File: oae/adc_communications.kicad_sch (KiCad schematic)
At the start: 2 parts

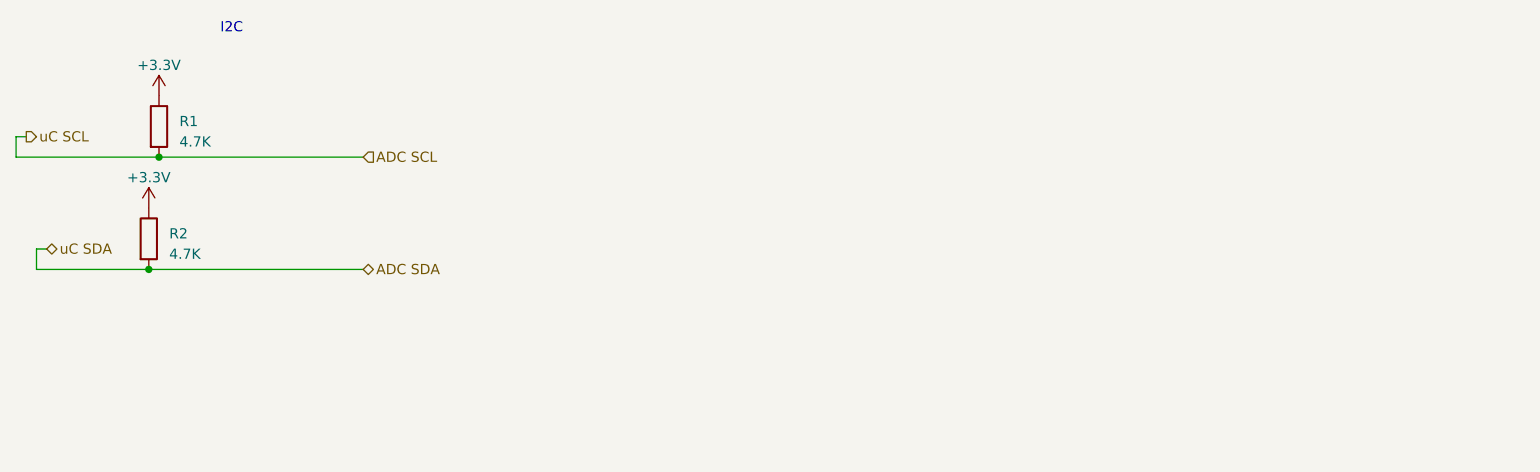
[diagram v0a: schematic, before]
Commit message: Changed resistor footprints
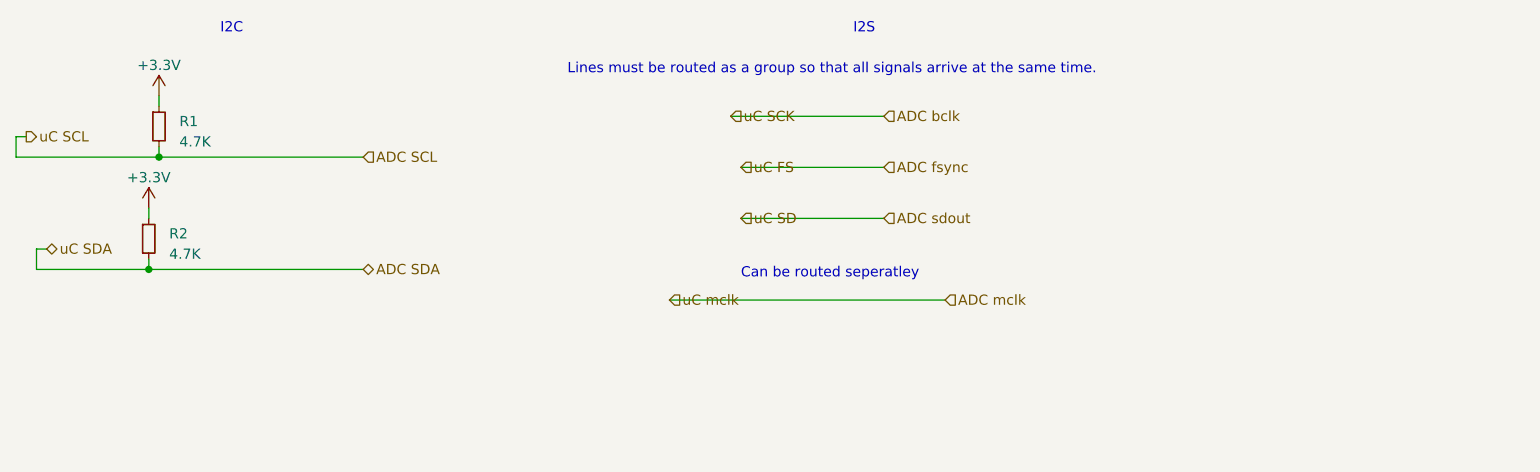
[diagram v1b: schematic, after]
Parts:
- R1: symbol Device:R -> Device:R_Small
- R2: footprint (none) -> Resistor_SMD:R_0603_1608Metric_Pad0.98x0.95mm_HandSolder; symbol Device:R -> Device:R_Small
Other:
- note added: "Can be routed seperatley"
- note added: "I2S"
- note added: "Lines must be routed as a group so that all signals arrive at the same time."
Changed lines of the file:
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@@
 (kicad_sch (version 20230121) (generator eeschema)
   (paper "A4")
+  (junction (at 95.25 80.01) (diameter 0) (color 0 0 0 0)
+  )
   (junction (at 93.98 93.98) (diameter 0) (color 0 0 0 0)
   )
-  (junction (at 95.25 80.01) (diameter 0) (color 0 0 0 0)
+  (wire (pts (xy 80.01 91.44) (xy 80.01 93.98))
+    (stroke (width 0) (type default))
   )
-  (wire (pts (xy 80.01 91.44) (xy 80.01 93.98))
+  (wire (pts (xy 95.25 72.39) (xy 95.25 73.66))
     (stroke (width 0) (type default))
   )
@@
     (stroke (width 0) (type default))
   )
+  (wire (pts (xy 95.25 80.01) (xy 120.65 80.01))
+    (stroke (width 0) (type default))
+  )
+  (wire (pts (xy 93.98 86.36) (xy 93.98 87.63))
+    (stroke (width 0) (type default))
+  )
+  (wire (pts (xy 95.25 78.74) (xy 95.25 80.01))
+    (stroke (width 0) (type default))
+  )
+  (wire (pts (xy 167.64 81.28) (xy 185.42 81.28))
+    (stroke (width 0) (type default))
+  )
+  (wire (pts (xy 166.37 74.93) (xy 185.42 74.93))
+    (stroke (width 0) (type default))
+  )
   (wire (pts (xy 80.01 93.98) (xy 93.98 93.98))
     (stroke (width 0) (type default))
   )
-  (wire (pts (xy 120.65 80.01) (xy 95.25 80.01))
+  (wire (pts (xy 93.98 93.98) (xy 120.65 93.98))
     (stroke (width 0) (type default))
   )
-  (wire (pts (xy 120.65 93.98) (xy 93.98 93.98))
+  (wire (pts (xy 93.98 92.71) (xy 93.98 93.98))
     (stroke (width 0) (type default))
   )
   (wire (pts (xy 77.47 80.01) (xy 95.25 80.01))
     (stroke (width 0) (type default))
+  )
+  (wire (pts (xy 167.64 87.63) (xy 185.42 87.63))
+    (stroke (width 0) (type default))
+  )
+  (wire (pts (xy 158.75 97.79) (xy 193.04 97.79))
+    (stroke (width 0) (type default))
+  )
+  (text "Can be routed seperatley" (at 167.64 95.25 0)
+    (effects (font (size 1.27 1.27)) (justify left bottom))
+  )
+  (text "I2S" (at 181.61 64.77 0)
+    (effects (font (size 1.27 1.27)) (justify left bottom))
+  )
+  (text "Lines must be routed as a group so that all signals arrive at the same time."
+    (at 146.05 69.85 0)
+    (effects (font (size 1.27 1.27)) (justify left bottom))
   )
   (text "I2C" (at 102.87 64.77 0)
@@
     (effects (font (size 1.27 1.27)) (justify left))
   )
+  (hierarchical_label "uC mclk" (shape input) (at 158.75 97.79 0) (fields_autoplaced)
+    (effects (font (size 1.27 1.27)) (justify left))
+  )
+  (hierarchical_label "uC SCK" (shape input) (at 166.37 74.93 0) (fields_autoplaced)
+    (effects (font (size 1.27 1.27)) (justify left))
+  )
+  (hierarchical_label "ADC sdout" (shape input) (at 185.42 87.63 0) (fields_autoplaced)
+    (effects (font (size 1.27 1.27)) (justify left))
+  )
+  (hierarchical_label "uC SD" (shape input) (at 167.64 87.63 0) (fields_autoplaced)
+    (effects (font (size 1.27 1.27)) (justify left))
+  )
   (hierarchical_label "ADC SCL" (shape input) (at 120.65 80.01 0) (fields_autoplaced)
+    (effects (font (size 1.27 1.27)) (justify left))
+  )
+  (hierarchical_label "uC FS" (shape input) (at 167.64 81.28 0) (fields_autoplaced)
+    (effects (font (size 1.27 1.27)) (justify left))
+  )
+  (hierarchical_label "ADC mclk" (shape input) (at 193.04 97.79 0) (fields_autoplaced)
+    (effects (font (size 1.27 1.27)) (justify left))
+  )
+  (hierarchical_label "ADC fsync" (shape input) (at 185.42 81.28 0) (fields_autoplaced)
+    (effects (font (size 1.27 1.27)) (justify left))
+  )
+  (hierarchical_label "ADC bclk" (shape input) (at 185.42 74.93 0) (fields_autoplaced)
     (effects (font (size 1.27 1.27)) (justify left))
   )
@@
     (effects (font (size 1.27 1.27)) (justify left))
   )
-  (symbol (lib_id "Device:R") (at 95.25 76.2 0) (unit 1)
+  (symbol (lib_id "Device:R_Small") (at 95.25 76.2 0) (unit 1)
     (in_bom yes) (on_board yes) (dnp no) (fields_autoplaced)
     (property "Reference" "R1" (at 97.79 75.565 0)
@@
       (effects (font (size 1.27 1.27)) (justify left))
     )
-    (property "Footprint" "" (at 93.472 76.2 90)
+    (property "Footprint" "" (at 95.25 76.2 0)
       (effects (font (size 1.27 1.27)) hide)
     )
@@
     )
   )
-  (symbol (lib_id "Device:R") (at 93.98 90.17 0) (unit 1)
+  (symbol (lib_id "Device:R_Small") (at 93.98 90.17 0) (unit 1)
     (in_bom yes) (on_board yes) (dnp no) (fields_autoplaced)
     (property "Reference" "R2" (at 96.52 89.535 0)
@@
       (effects (font (size 1.27 1.27)) (justify left))
     )
-    (property "Footprint" "" (at 92.202 90.17 90)
+    (property "Footprint" "Resistor_SMD:R_0603_1608Metric_Pad0.98x0.95mm_HandSolder" (at 93.98 90.17 0)
       (effects (font (size 1.27 1.27)) hide)
     )

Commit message: Add ADC + power wiring into schematic
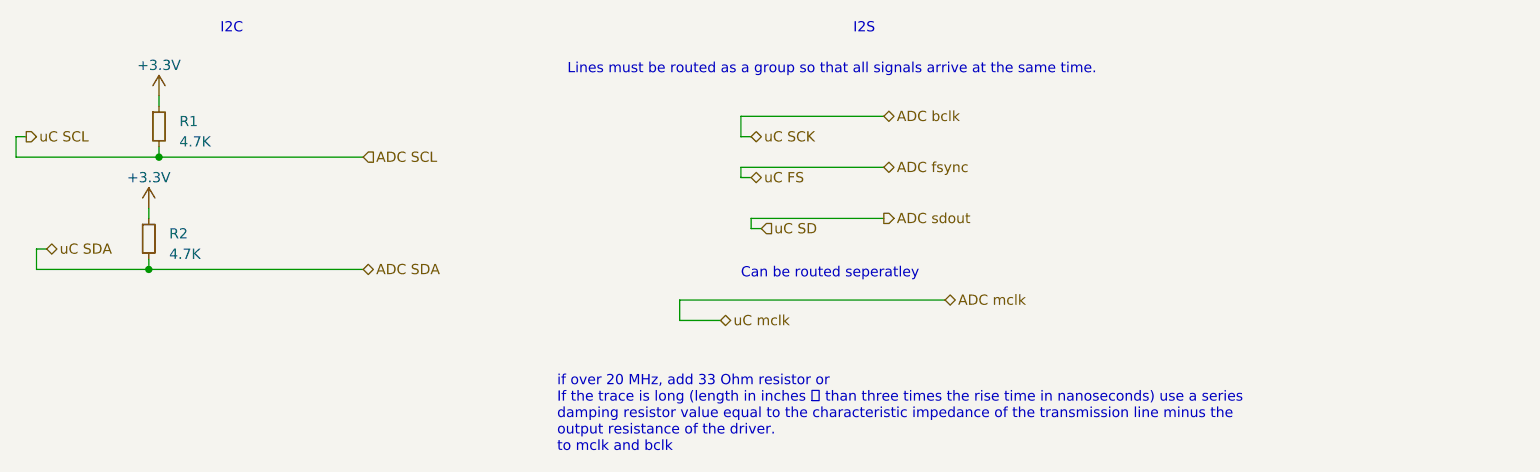
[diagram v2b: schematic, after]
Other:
- note added: "if over 20 MHz, add 33 Ohm resistor or If the trace is long (length in inches  than three times the rise time in nanoseconds) use a series damping resistor value equal to the characteristic impedance of the transmission line minus the output resistance of the driver. to mclk and bclk"
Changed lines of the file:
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@@
   (junction (at 93.98 93.98) (diameter 0) (color 0 0 0 0)
   )
+  (wire (pts (xy 168.91 88.9) (xy 168.91 87.63))
+    (stroke (width 0) (type default))
+  )
   (wire (pts (xy 80.01 91.44) (xy 80.01 93.98))
+    (stroke (width 0) (type default))
+  )
+  (wire (pts (xy 167.64 82.55) (xy 167.64 81.28))
     (stroke (width 0) (type default))
   )
@@
   )
   (wire (pts (xy 78.74 77.47) (xy 77.47 77.47))
+    (stroke (width 0) (type default))
+  )
+  (wire (pts (xy 168.91 87.63) (xy 185.42 87.63))
     (stroke (width 0) (type default))
   )
@@
     (stroke (width 0) (type default))
   )
-  (wire (pts (xy 167.64 81.28) (xy 185.42 81.28))
+  (wire (pts (xy 168.91 82.55) (xy 167.64 82.55))
     (stroke (width 0) (type default))
   )
-  (wire (pts (xy 166.37 74.93) (xy 185.42 74.93))
+  (wire (pts (xy 168.91 77.47) (xy 167.64 77.47))
     (stroke (width 0) (type default))
   )
@@
     (stroke (width 0) (type default))
   )
-  (wire (pts (xy 167.64 87.63) (xy 185.42 87.63))
+  (wire (pts (xy 170.18 88.9) (xy 168.91 88.9))
     (stroke (width 0) (type default))
   )
-  (wire (pts (xy 158.75 97.79) (xy 193.04 97.79))
+  (wire (pts (xy 167.64 81.28) (xy 185.42 81.28))
     (stroke (width 0) (type default))
+  )
+  (wire (pts (xy 165.1 100.33) (xy 160.02 100.33))
+    (stroke (width 0) (type default))
+  )
+  (wire (pts (xy 167.64 77.47) (xy 167.64 74.93))
+    (stroke (width 0) (type default))
+  )
+  (wire (pts (xy 160.02 97.79) (xy 193.04 97.79))
+    (stroke (width 0) (type default))
+  )
+  (wire (pts (xy 160.02 100.33) (xy 160.02 97.79))
+    (stroke (width 0) (type default))
+  )
+  (wire (pts (xy 167.64 74.93) (xy 185.42 74.93))
+    (stroke (width 0) (type default))
+  )
+  (text "if over 20 MHz, add 33 Ohm resistor or \nIf the trace is long (length in inches  than three times the rise time in nanoseconds) use a series\ndamping resistor value equal to the characteristic impedance of the transmission line minus the\noutput resistance of the driver.\nto mclk and bclk"
+    (at 144.78 116.84 0)
+    (effects (font (size 1.27 1.27)) (justify left bottom))
   )
   (text "Can be routed seperatley" (at 167.64 95.25 0)
@@
     (effects (font (size 1.27 1.27)) (justify left))
   )
-  (hierarchical_label "uC mclk" (shape input) (at 158.75 97.79 0) (fields_autoplaced)
+  (hierarchical_label "uC mclk" (shape bidirectional) (at 165.1 100.33 0) (fields_autoplaced)
     (effects (font (size 1.27 1.27)) (justify left))
   )
-  (hierarchical_label "uC SCK" (shape input) (at 166.37 74.93 0) (fields_autoplaced)
+  (hierarchical_label "uC SCK" (shape bidirectional) (at 168.91 77.47 0) (fields_autoplaced)
     (effects (font (size 1.27 1.27)) (justify left))
   )
-  (hierarchical_label "ADC sdout" (shape input) (at 185.42 87.63 0) (fields_autoplaced)
+  (hierarchical_label "ADC sdout" (shape output) (at 185.42 87.63 0) (fields_autoplaced)
     (effects (font (size 1.27 1.27)) (justify left))
   )
-  (hierarchical_label "uC SD" (shape input) (at 167.64 87.63 0) (fields_autoplaced)
+  (hierarchical_label "uC SD" (shape input) (at 170.18 88.9 0) (fields_autoplaced)
     (effects (font (size 1.27 1.27)) (justify left))
   )
@@
     (effects (font (size 1.27 1.27)) (justify left))
   )
-  (hierarchical_label "uC FS" (shape input) (at 167.64 81.28 0) (fields_autoplaced)
+  (hierarchical_label "uC FS" (shape bidirectional) (at 168.91 82.55 0) (fields_autoplaced)
     (effects (font (size 1.27 1.27)) (justify left))
   )
-  (hierarchical_label "ADC mclk" (shape input) (at 193.04 97.79 0) (fields_autoplaced)
+  (hierarchical_label "ADC mclk" (shape bidirectional) (at 193.04 97.79 0) (fields_autoplaced)
     (effects (font (size 1.27 1.27)) (justify left))
   )
-  (hierarchical_label "ADC fsync" (shape input) (at 185.42 81.28 0) (fields_autoplaced)
+  (hierarchical_label "ADC fsync" (shape bidirectional) (at 185.42 81.28 0) (fields_autoplaced)
     (effects (font (size 1.27 1.27)) (justify left))
   )
-  (hierarchical_label "ADC bclk" (shape input) (at 185.42 74.93 0) (fields_autoplaced)
+  (hierarchical_label "ADC bclk" (shape bidirectional) (at 185.42 74.93 0) (fields_autoplaced)
     (effects (font (size 1.27 1.27)) (justify left))
   )

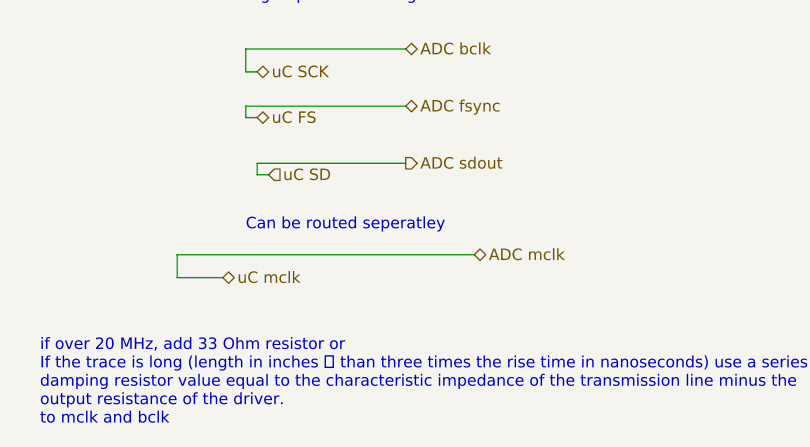
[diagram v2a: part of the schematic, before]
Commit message: Add jumpers for ADC GPIO pins
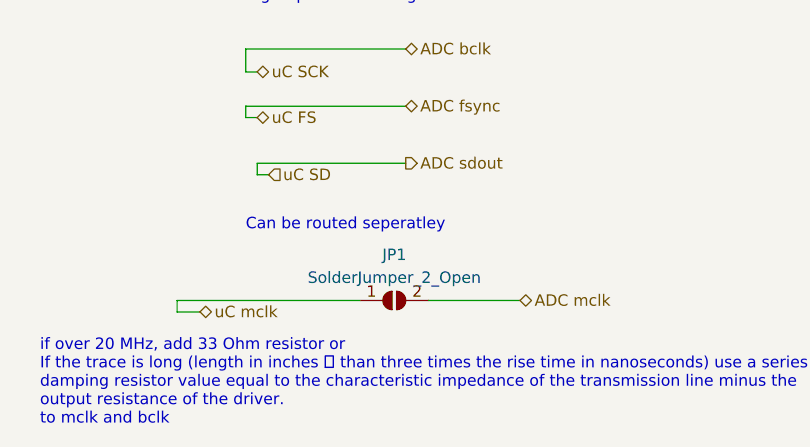
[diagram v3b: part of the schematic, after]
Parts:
- added JP1: SolderJumper_2_Open, Jumper:SolderJumper-2_P1.3mm_Open_Pad1.0x1.5mm, symbol Jumper:SolderJumper_2_Open
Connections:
- net ADC mclk: now also JP1.2 (B)
- new net uC mclk: JP1.1 (A)
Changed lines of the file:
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@@
+    (stroke (width 0) (type default))
+  )
+  (wire (pts (xy 187.96 102.87) (xy 198.12 102.87))
     (stroke (width 0) (type default))
   )
@@
     (stroke (width 0) (type default))
   )
-  (wire (pts (xy 165.1 100.33) (xy 160.02 100.33))
+  (wire (pts (xy 160.02 104.14) (xy 160.02 102.87))
+    (stroke (width 0) (type default))
+  )
+  (wire (pts (xy 162.56 104.14) (xy 160.02 104.14))
     (stroke (width 0) (type default))
   )
@@
     (stroke (width 0) (type default))
   )
-  (wire (pts (xy 160.02 97.79) (xy 193.04 97.79))
-    (stroke (width 0) (type default))
-  )
-  (wire (pts (xy 160.02 100.33) (xy 160.02 97.79))
+  (wire (pts (xy 160.02 102.87) (xy 180.34 102.87))
     (stroke (width 0) (type default))
   )
@@
     (effects (font (size 1.27 1.27)) (justify left))
   )
-  (hierarchical_label "uC mclk" (shape bidirectional) (at 165.1 100.33 0) (fields_autoplaced)
+  (hierarchical_label "uC mclk" (shape bidirectional) (at 162.56 104.14 0) (fields_autoplaced)
     (effects (font (size 1.27 1.27)) (justify left))
   )
@@
     (effects (font (size 1.27 1.27)) (justify left))
   )
-  (hierarchical_label "ADC mclk" (shape bidirectional) (at 193.04 97.79 0) (fields_autoplaced)
+  (hierarchical_label "ADC mclk" (shape bidirectional) (at 198.12 102.87 0) (fields_autoplaced)
     (effects (font (size 1.27 1.27)) (justify left))
   )
@@
     (effects (font (size 1.27 1.27)) (justify left))
   )
+  (symbol (lib_id "Jumper:SolderJumper_2_Open") (at 184.15 102.87 0) (unit 1)
+    (in_bom yes) (on_board yes) (dnp no) (fields_autoplaced)
+    (property "Reference" "JP1" (at 184.15 97.79 0)
+      (effects (font (size 1.27 1.27)))
+    )
+    (property "Value" "SolderJumper_2_Open" (at 184.15 100.33 0)
+      (effects (font (size 1.27 1.27)))
+    )
+    (property "Footprint" "Jumper:SolderJumper-2_P1.3mm_Open_Pad1.0x1.5mm" (at 184.15 102.87 0)
+      (effects (font (size 1.27 1.27)) hide)
+    )
+    (property "Datasheet" "~" (at 184.15 102.87 0)
+      (effects (font (size 1.27 1.27)) hide)
+    )
+    (pin "1")
+    (pin "2")
+    (instances
+      (project "oae"
+        (path "/e63e39d7-6ac0-4ffd-8aa3-1841a4541b55/f5ec4301-2f32-46c4-8f0d-2c5a15cb6fc4/2604763a-d7f3-46e8-b8fe-c57329b542da"
+          (reference "JP1") (unit 1)
+        )
+      )
+    )
+  )
   (symbol (lib_id "Device:R_Small") (at 95.25 76.2 0) (unit 1)
